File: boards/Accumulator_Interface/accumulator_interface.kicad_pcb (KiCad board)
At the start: 2 copper layers, 13 parts, among them J1 INTERNAL, J10 AIR_CTRL_18, J11 Energy_Meter_Power, J2 EXTERNAL, J3 AIR_CTRL, J4 IMD_LATCH, J5 DISCHARGE, J6 BMS_Master, J7 BMS, J8 TSAL/AIL, J9 IMD_LATCH, U1 RJ45_VT_AIR, U2 RJ45_VT_BMS

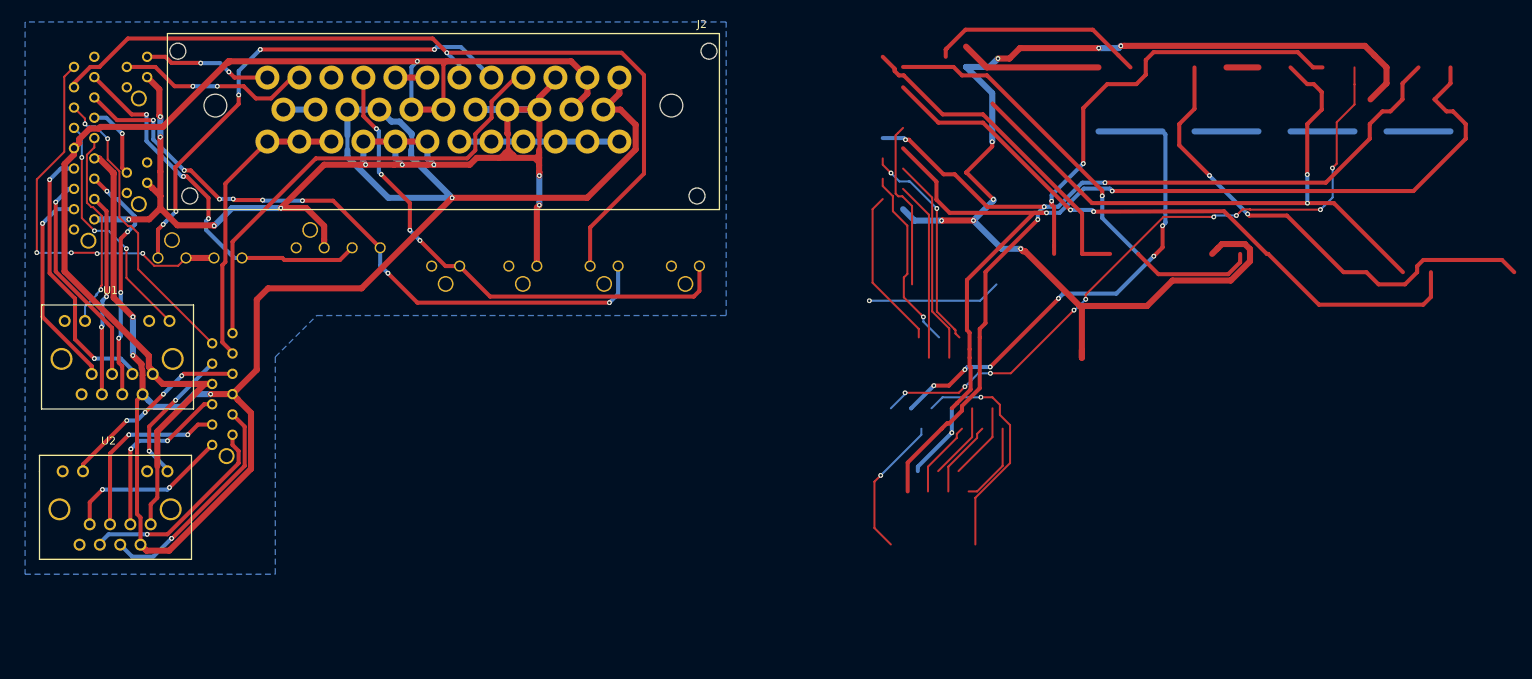
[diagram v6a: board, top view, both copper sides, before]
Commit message: finished tracing. Adding text
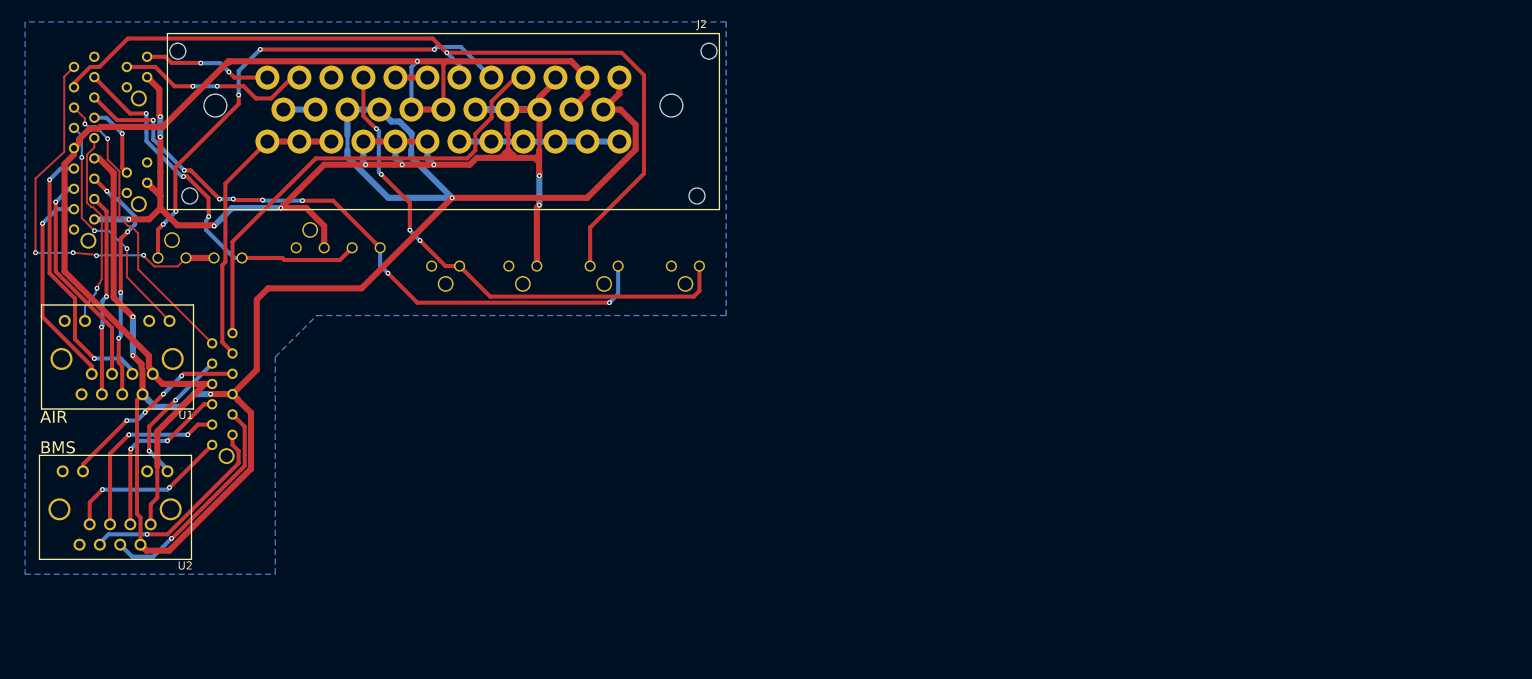
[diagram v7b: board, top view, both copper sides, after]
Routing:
- net (no net): track 1261.2 -> 0.00 mm, vias 45 -> 0
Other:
- board text added: "AIR"
- board text added: "AIR_CTRL"
- board text added: "BMS"
- board text added: "DISCHARGE"
- board text added: "E_METER"
- board text added: "IMD_LATCH"
- board text removed: "12V"

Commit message: added a cad for the board
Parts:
- added G***: LOGO, footprints:Logo_Large, F.Cu at (100.9, 62.8)
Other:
- board outline added: 93 x 73.7 mm
- board text added: "12V"
- board text added: "GND"
- board text added: "Josh Deng, William Fairman - Rev_1"
- board text added: "TSAL/AIL"
- board text removed: "HVD_OUT"
- board text removed: "MAIN_PACK_OUT"
- board text removed: "TSMS_IN"
